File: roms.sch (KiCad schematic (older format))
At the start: 20 parts, among them CN20 TA11, J4 128/256k, J6 128/256k, J7 SolderJumper_3_Bridged12, U18 2364, U32 23128, U33 23128, U34 23128, U35 318020-03, U36 23256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

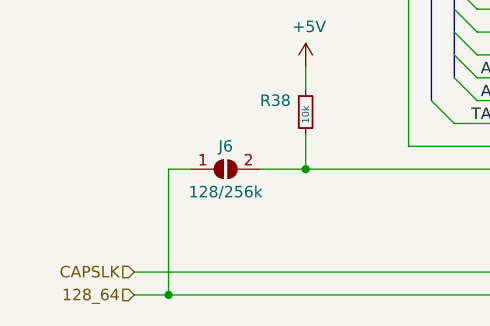
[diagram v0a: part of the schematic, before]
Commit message: Clean up schematic
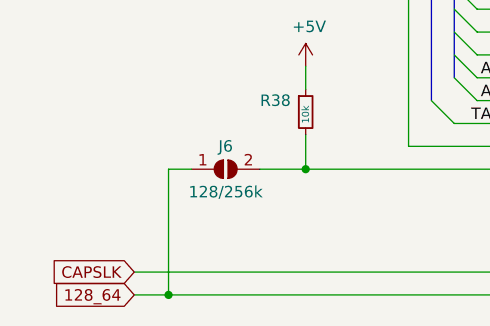
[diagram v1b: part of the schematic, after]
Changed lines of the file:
@@
 Text HLabel 1000 3550 0    50   Input ~ 0
 TA[8..15]
-Text HLabel 1000 6450 0    50   Input ~ 0
-128_64
 $Comp
 L Jumper:SolderJumper_2_Open J6
@@
 Wire Wire Line
 	9400 2850 9400 2900
-Text HLabel 1000 6350 0    50   Input ~ 0
-CAPSLK
 Wire Wire Line
 	1000 6450 1150 6450
@@
 Wire Bus Line
 	5400 1350 5400 3750
+Text GLabel 1000 6450 0    50   Input ~ 0
+128_64
+Text GLabel 1000 6350 0    50   Input ~ 0
+CAPSLK
 $EndSCHEMATC
